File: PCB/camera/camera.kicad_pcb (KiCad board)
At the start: 2 copper layers, 45 x 65 mm, 16 parts, among them J1 Conn_01x02, J2 Conn_01x04, J3 Conn_01x02, U1 NRF24L01_Breakout, U2 LM7805

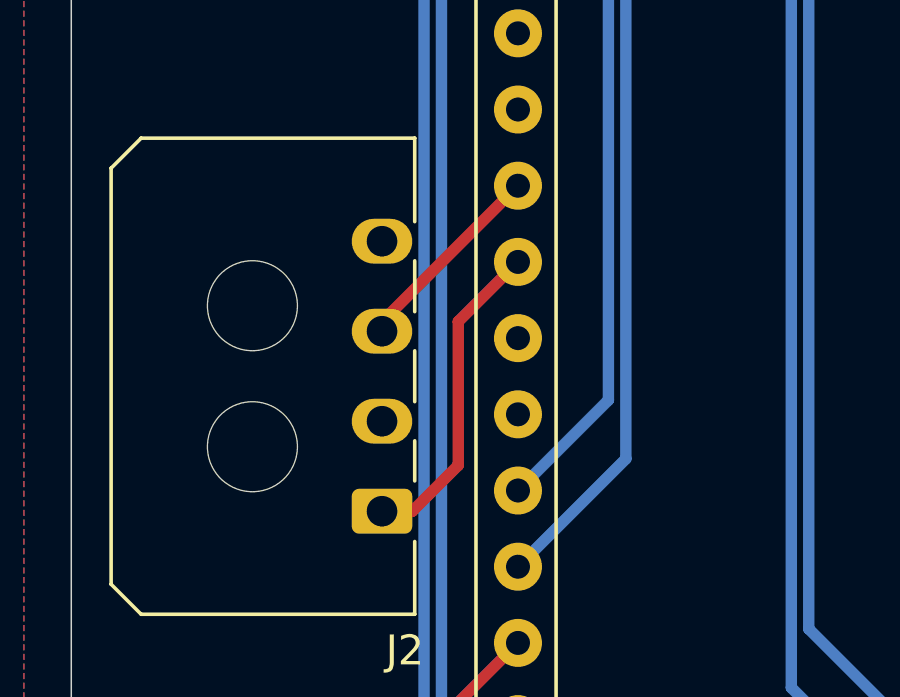
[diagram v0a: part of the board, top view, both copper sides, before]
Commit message: minor tweaks and added completed vibration board - schematic and routing
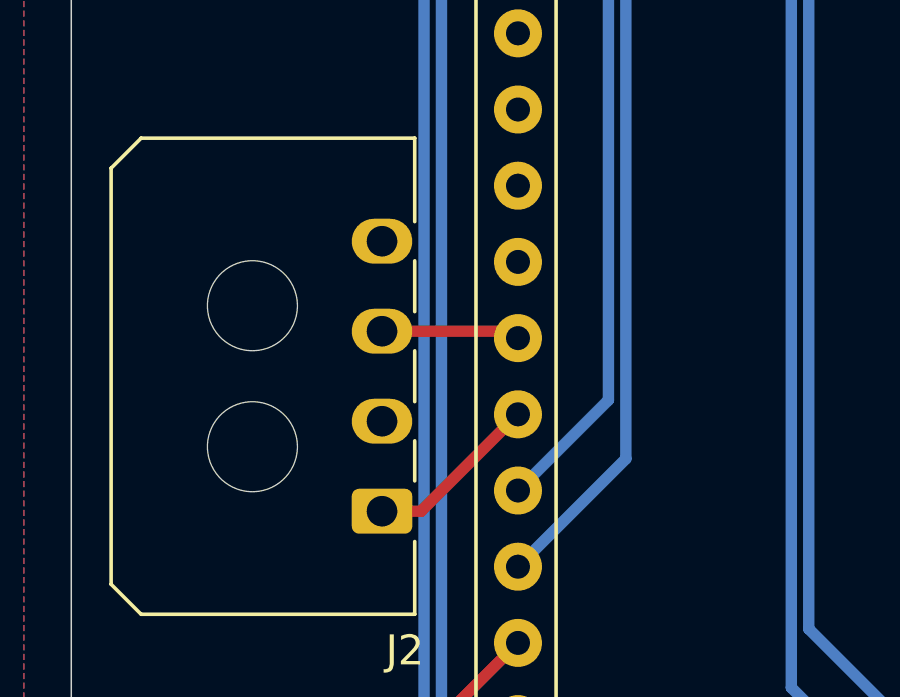
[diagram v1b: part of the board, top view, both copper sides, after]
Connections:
- A1 pad 6: D3 -> (no net)
- A1 pad 7: D4 -> (no net)
- A1 pad 8: (no net) -> D5
- A1 pad 9: (no net) -> D6
- J2 pad 1: D4 -> D6
- J2 pad 3: D3 -> D5
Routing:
- net D4: track 10.8 -> 0.00 mm
- net D3: track 6.73 -> 0.00 mm
- net D6: track 0.00 -> 5.87 mm
- net D5: track 0.00 -> 4.95 mm

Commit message: Camera review complete. Create gerbers
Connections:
- J2 pad 1: D6 -> GND
- J2 pad 2: GND -> D6
- J2 pad 3: D5 -> GND
- J2 pad 4: GND -> D5
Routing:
- net D5: track 4.95 -> 6.25 mm
- net D6: track 5.87 -> 4.63 mm
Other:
- board text added: "-"
- board text added: "5V Out"
- board text added: "V in"
- board text added: "V1.0"
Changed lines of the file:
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@@
   (general
     (thickness 1.6)
-    (drawings 8)
-    (tracks 64)
+    (drawings 13)
+    (tracks 65)
     (zones 0)
     (modules 16)
@@
   )
   (setup
-    (last_trace_width 0.381)
+    (last_trace_width 1.524)
     (user_trace_width 1.27)
     (user_trace_width 1.524)
@@
       (outputformat 1)
       (mirror false)
-      (drillshape 1)
+      (drillshape 0)
       (scaleselection 1)
-      (outputdirectory ""))
+      (outputdirectory "Camera-Gerber/"))
   )
   (net 0 "")
@@
     (descr "nRF24L01 breakout board")
     (tags "nRF24L01 adapter breakout")
-    (fp_text reference U1 (at 28.829 12.885) (layer F.SilkS)
+    (fp_text reference U1 (at -2.952 12.954) (layer F.SilkS)
       (effects (font (size 1 1) (thickness 0.15)))
     )
@@
     (pad "" np_thru_hole circle (at 6.85 -4.32 90) (size 3 3) (drill 3) (layers *.Cu *.Mask))
     (pad 1 thru_hole roundrect (at 0 0 90) (size 1.5 2.02) (drill 1.02) (layers *.Cu *.Mask) (roundrect_rratio 0.166667)
+      (net 2 GND))
+    (pad 2 thru_hole oval (at 3 0 90) (size 1.5 2.02) (drill 1.02) (layers *.Cu *.Mask)
       (net 15 D6))
-    (pad 2 thru_hole oval (at 3 0 90) (size 1.5 2.02) (drill 1.02) (layers *.Cu *.Mask)
-      (net 2 GND))
     (pad 3 thru_hole oval (at 6 0 90) (size 1.5 2.02) (drill 1.02) (layers *.Cu *.Mask)
+      (net 2 GND))
+    (pad 4 thru_hole oval (at 9 0 90) (size 1.5 2.02) (drill 1.02) (layers *.Cu *.Mask)
       (net 14 D5))
-    (pad 4 thru_hole oval (at 9 0 90) (size 1.5 2.02) (drill 1.02) (layers *.Cu *.Mask)
-      (net 2 GND))
     (model ${KISYS3DMOD}/Connector_Molex.3dshapes/Molex_Micro-Fit_3.0_43650-0400_1x04_P3.00mm_Horizontal.wrl
       (at (xyz 0 0 0))
@@
     (tags "CMS SOT")
     (attr smd)
-    (fp_text reference U2 (at 0 -4.5) (layer F.SilkS)
+    (fp_text reference U2 (at 3.616 4.577) (layer F.SilkS)
       (effects (font (size 1 1) (thickness 0.15)))
     )
@@
       (rotate (xyz 0 0 0))
     )
+  )
+  (gr_text "5V Out" (at 98.298 129.794) (layer F.SilkS)
+    (effects (font (size 1.5 1.5) (thickness 0.3)))
+  )
+  (gr_text "V in" (at 101.6 101.854) (layer F.SilkS)
+    (effects (font (size 1.5 1.5) (thickness 0.3)))
+  )
+  (gr_text V1.0 (at 61.722 102.108 270) (layer F.SilkS)
+    (effects (font (size 1.5 1.5) (thickness 0.3)))
+  )
+  (gr_text - (at 72.136 124.46 90) (layer F.SilkS)
+    (effects (font (size 1.5 1.5) (thickness 0.3)))
+  )
+  (gr_text - (at 72.136 130.556 90) (layer F.SilkS)
+    (effects (font (size 1.5 1.5) (thickness 0.3)))
   )
   (dimension 57 (width 0.15) (layer F.Fab)
@@
   (segment (start 72.33952 137.40352) (end 74.89 139.954) (width 0.381) (layer B.Cu) (net 7) (status 20))
   (segment (start 72.33952 98.283848) (end 72.33952 137.40352) (width 0.381) (layer B.Cu) (net 7))
-  (segment (start 95.833 119.344) (end 93.726 119.344) (width 1.524) (layer F.Cu) (net 8) (status 30))
-  (segment (start 96.358 119.869) (end 95.833 119.344) (width 1.524) (layer F.Cu) (net 8) (status 30))
   (segment (start 91.728 106.934) (end 94.488 109.694) (width 1.524) (layer F.Cu) (net 8) (status 20))
   (segment (start 90.13 106.934) (end 91.728 106.934) (width 1.524) (layer F.Cu) (net 8) (status 10))
-  (segment (start 94.488 118.582) (end 93.726 119.344) (width 1.524) (layer F.Cu) (net 8) (status 20))
-  (segment (start 94.488 109.694) (end 94.488 118.582) (width 1.524) (layer F.Cu) (net 8) (status 10))
+  (segment (start 95.833 119.344) (end 96.358 119.869) (width 1.524) (layer F.Cu) (net 8))
+  (segment (start 93.726 119.344) (end 95.833 119.344) (width 1.524) (layer F.Cu) (net 8))
+  (segment (start 94.488 118.582) (end 93.726 119.344) (width 1.524) (layer F.Cu) (net 8))
+  (segment (start 94.488 109.694) (end 94.488 118.582) (width 1.524) (layer F.Cu) (net 8))
   (segment (start 74.090001 141.694001) (end 74.89 142.494) (width 0.381) (layer B.Cu) (net 9) (status 20))
   (segment (start 71.75851 139.36251) (end 74.090001 141.694001) (width 0.381) (layer B.Cu) (net 9))
@@
   (segment (start 69.896 146.304) (end 69.896 148.279) (width 0.381) (layer F.Cu) (net 11) (status 30))
   (segment (start 93.359 146.304) (end 93.359 148.324) (width 0.381) (layer F.Cu) (net 12) (status 30))
-  (segment (start 70.358 124.166) (end 70.358 124.484) (width 0.381) (layer F.Cu) (net 14) (status 30))
   (segment (start 95.833 124.994) (end 93.726 124.994) (width 1.524) (layer F.Cu) (net 13) (status 30))
   (segment (start 96.358 124.469) (end 95.833 124.994) (width 1.524) (layer F.Cu) (net 13) (status 30))
@@
   (segment (start 91.954 126.291) (end 91.954 135.37) (width 1.524) (layer F.Cu) (net 13))
   (segment (start 93.726 124.994) (end 93.251 124.994) (width 1.524) (layer F.Cu) (net 13) (status 30))
-  (segment (start 74.66 124.484) (end 74.89 124.714) (width 0.381) (layer F.Cu) (net 14))
-  (segment (start 70.358 124.484) (end 74.66 124.484) (width 0.381) (layer F.Cu) (net 14))
-  (segment (start 71.66 130.484) (end 70.358 130.484) (width 0.381) (layer F.Cu) (net 15))
-  (segment (start 74.89 127.254) (end 71.66 130.484) (width 0.381) (layer F.Cu) (net 15))
+  (segment (start 74.66 124.484) (end 74.89 124.714) (width 0.381) (layer F.Cu) (net 14) (status 30))
+  (segment (start 71.749 121.484) (end 74.89 124.625) (width 0.381) (layer F.Cu) (net 14))
+  (segment (start 74.89 124.625) (end 74.89 124.714) (width 0.381) (layer F.Cu) (net 14))
+  (segment (start 70.358 121.484) (end 71.749 121.484) (width 0.381) (layer F.Cu) (net 14))
+  (segment (start 74.66 127.484) (end 74.89 127.254) (width 0.381) (layer F.Cu) (net 15))
+  (segment (start 70.358 127.484) (end 74.66 127.484) (width 0.381) (layer F.Cu) (net 15))
   (zone (net 2) (net_name GND) (layer B.Cu) (hatch edge 0.508)
     (connect_pads (clearance 0.254))
